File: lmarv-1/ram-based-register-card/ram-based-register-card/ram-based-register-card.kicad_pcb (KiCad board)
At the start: 4 copper layers, 125.4 x 41.3 mm, 17 parts, among them P1 dual-pcie-cardedge, U1 IDT70V24_TQ100, U2 IDT70V24_TQ100, U3 IDT70V24_TQ100, U4 IDT70V24_TQ100

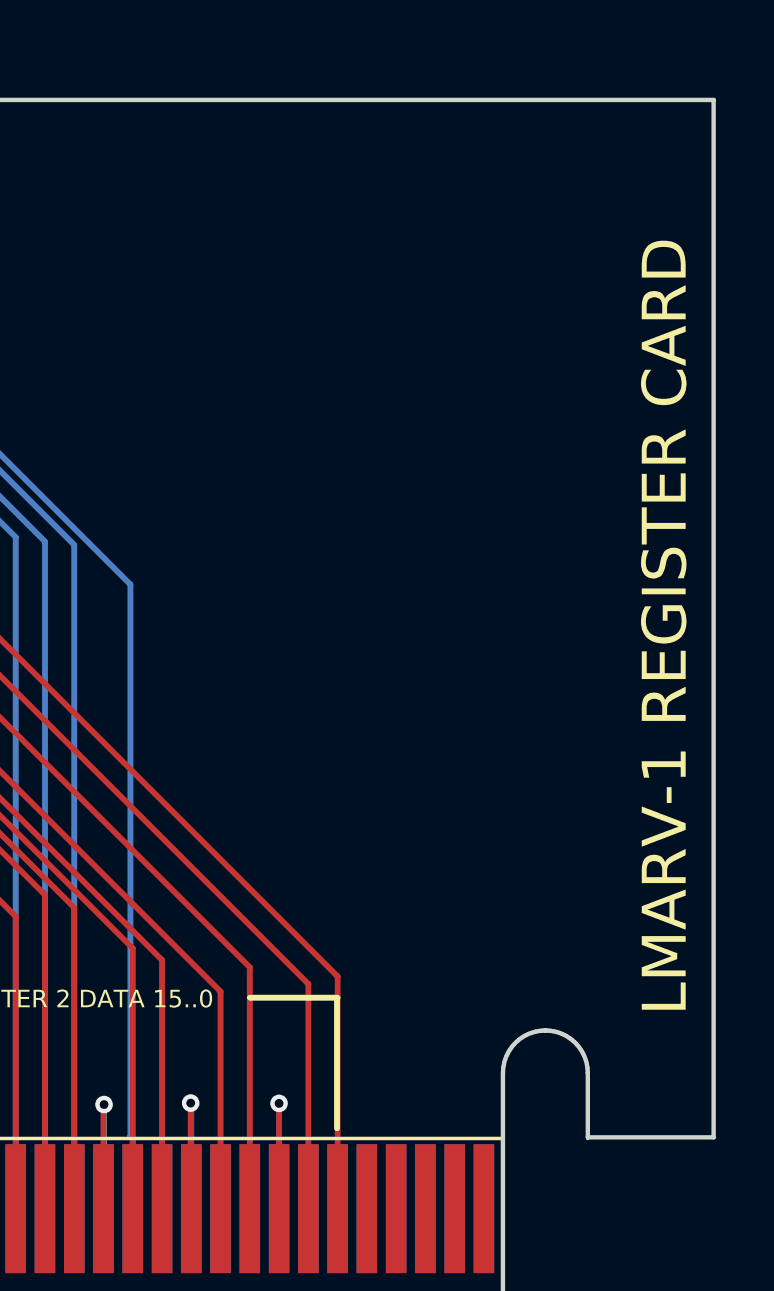
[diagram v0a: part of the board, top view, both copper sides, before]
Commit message: Updates silkscreen and gerbers for register card
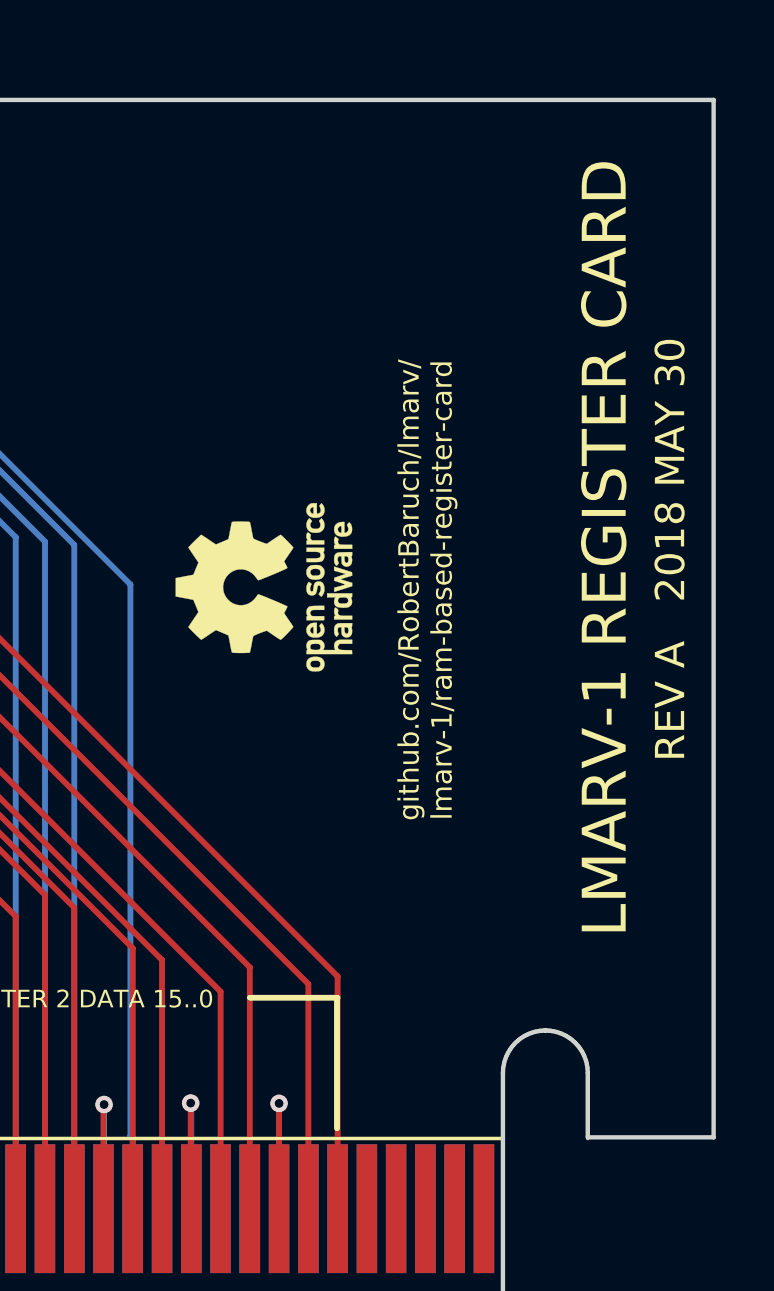
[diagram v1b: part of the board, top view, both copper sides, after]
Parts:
- added REF***: OSHW-Logo_5.7x6mm_SilkScreen, Symbols:OSHW-Logo_5.7x6mm_SilkScreen, F.Cu at (164.4, 58.5)
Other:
- board text added: "REV A 2018 MAY 30"
- board text added: "github.com/RobertBaruch/lmarv/ lmarv-1/ram-based-register-card"
